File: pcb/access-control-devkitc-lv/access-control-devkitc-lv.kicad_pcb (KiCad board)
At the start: 2 copper layers, 71.4 x 65.5 mm, 41 parts, among them J1 CON_I2C, K1 G5LE-1, U1 ESP32-DevKitC

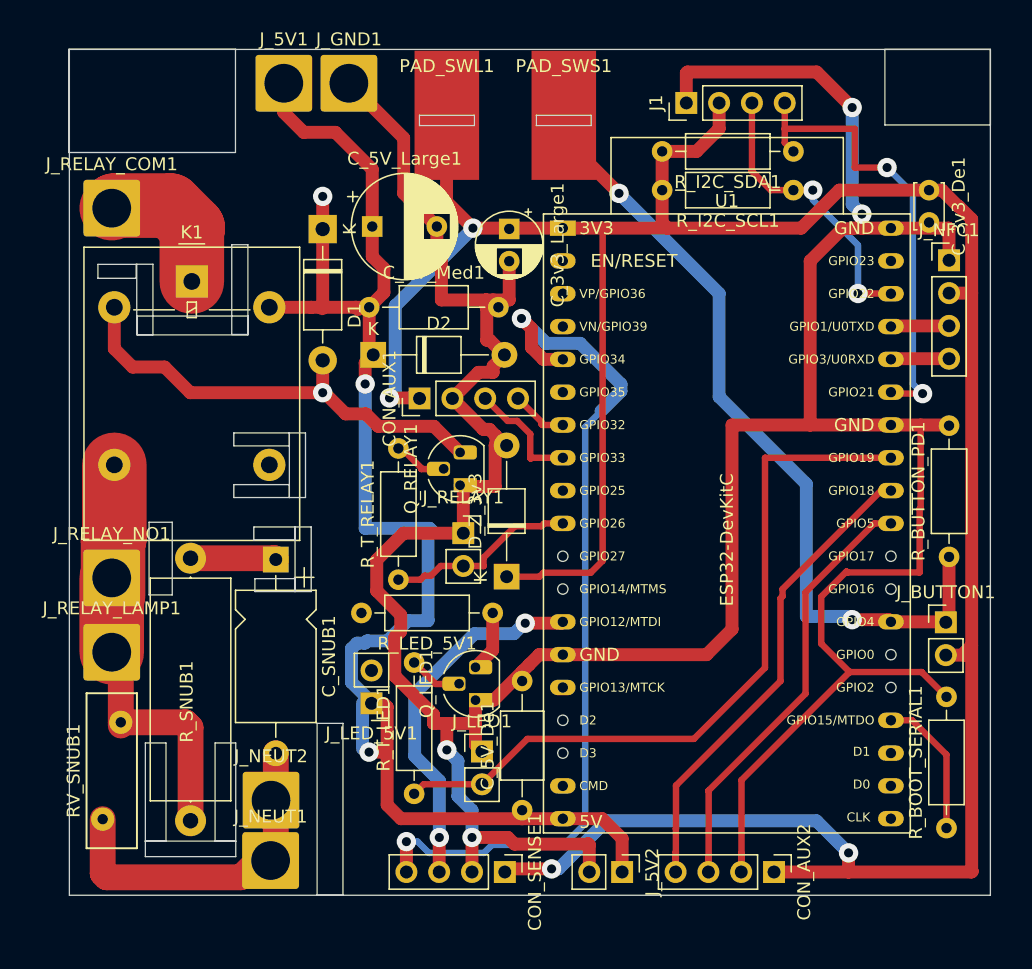
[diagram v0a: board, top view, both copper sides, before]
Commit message: Split board into Low Voltage / Relay modules
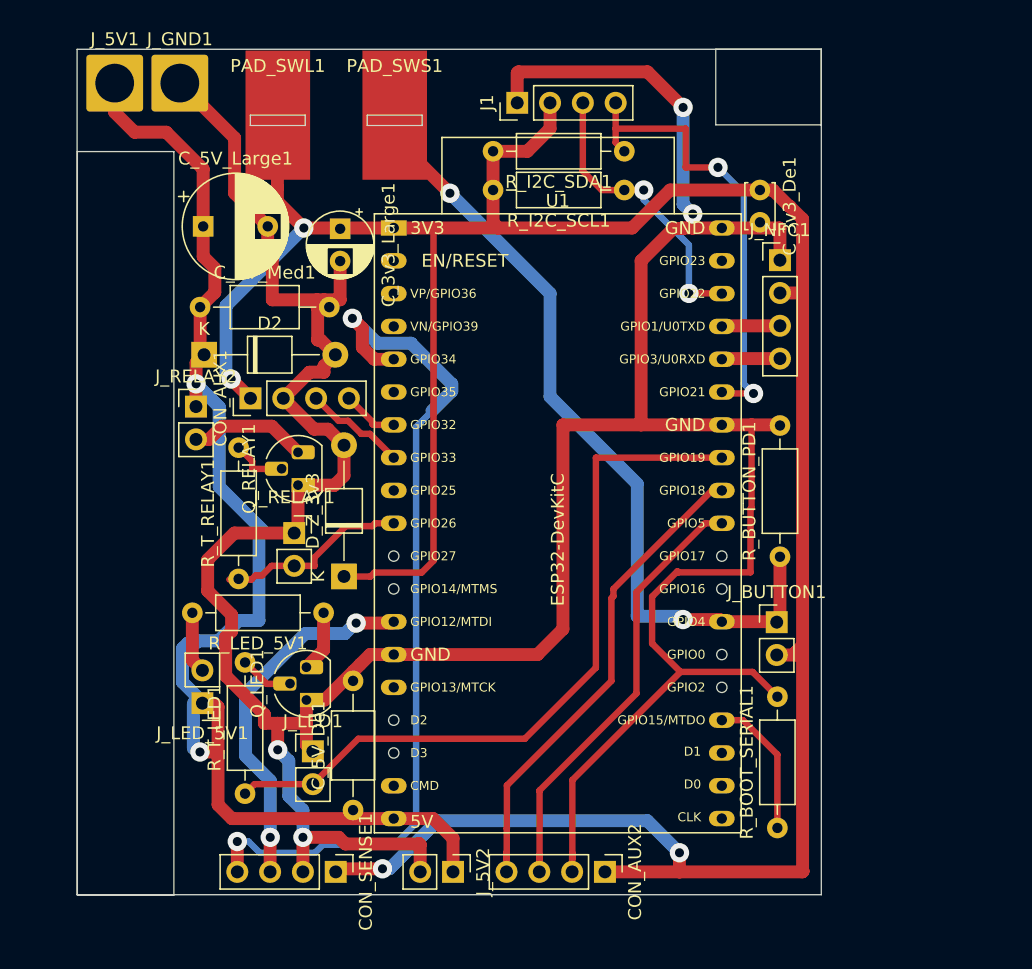
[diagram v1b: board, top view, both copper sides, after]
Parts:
- removed C_SNUB1: C, Capacitor_THT:CP_Axial_L10.0mm_D6.0mm_P15.00mm_Horizontal
- removed D1: 1N4007, Diode_THT:D_DO-41_SOD81_P10.16mm_Horizontal
- removed J_NEUT1, J_NEUT2, J_RELAY_COM1, J_RELAY_LAMP1, J_RELAY_NO1: Conn_01x01_Socket, Connector_Wire:SolderWire-2.5sqmm_1x01_D2.4mm_OD4.4mm
- removed K1: G5LE-1, Relay_THT:Relay_SPDT_Omron-G5LE-1
- removed RV_SNUB1: Varistor, Varistor:RV_Disc_D12mm_W3.9mm_P7.5mm
- removed R_SNUB1: R, Resistor_THT:R_Axial_DIN0617_L17.0mm_D6.0mm_P20.32mm_Horizontal
- added J_RELAY2: Conn_01x02_Socket, Connector_PinHeader_2.54mm:PinHeader_1x02_P2.54mm_Vertical, F.Cu at (9.20, 27.6)
- moved CON_AUX2 13.1 mm to (40.9, 63.7)
- moved C_3v3_De1 13.1 mm to (52.9, 10.9)
- moved C_3v3_Large1 13.1 mm to (20.4, 13.9)
- moved C_5V_De1 13.1 mm to (21.4, 58.9)
- moved J_BUTTON1 13.1 mm to (54.2, 44.3)
- moved J_NFC1 13.1 mm to (54.4, 16.3)
- moved R_BUTTON_PD1 13.1 mm to (54.4, 39.3)
- moved R_I2C_SCL1 13.1 mm to (42.4, 10.9)
- moved R_I2C_SDA1 13.1 mm to (42.4, 7.88)
- moved R_LED_5V1 13.1 mm to (19.1, 43.6)
- moved CON_AUX1 13.1 mm to (13.4, 27.0)
- moved C_5V_Large1 13.1 mm to (9.76, 13.7)
- moved D2 13.1 mm to (9.83, 23.6)
- moved CON_SENSE1 13.1 mm to (20.0, 63.7)
- moved C_5V_Med1 13.1 mm to (9.52, 19.9)
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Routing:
- net Net-(J_RELAY_LAMP1-Pin_1): track 36.5 -> 0.00 mm
- net Net-(J_RELAY2-Pin_2): track 35.8 -> 9.16 mm, vias 1 -> 0
- net NEUT: track 25.0 -> 0.00 mm
- net +5V: track 116.2 -> 98.3 mm, vias 3 -> 2
- net Net-(J_RELAY_COM1-Pin_1): track 11.2 -> 0.00 mm
- net Net-(C_SNUB1-Pad1): track 6.78 -> 0.00 mm
- net Net-(J_LED_5V1-Pin_2): track 0.00 -> 4.78 mm
- net +3V3: track 215.8 -> 214.1 mm
- net GND: track 270.1 -> 271.4 mm
- net Net-(CON_AUX1-Pin_3): track 9.06 -> 7.91 mm
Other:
- board size 71.4 x 65.5 mm -> 57.6 x 65.5 mm

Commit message: Update with values
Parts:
- removed J_GND1: Conn_01x01_Socket, Connector_Wire:SolderWire-2.5sqmm_1x01_D2.4mm_OD4.4mm
- C_5V_De1: footprint Capacitor_THT:C_Axial_L5.1mm_D3.1mm_P10.00mm_Horizontal -> Capacitor_THT:C_Disc_D4.3mm_W1.9mm_P5.00mm
- C_5V_Med1: footprint Capacitor_THT:C_Axial_L5.1mm_D3.1mm_P10.00mm_Horizontal -> Capacitor_THT:C_Disc_D5.0mm_W2.5mm_P5.00mm
- J_5V1: value Conn_01x01_Socket -> Conn_01x02_Socket; footprint Connector_Wire:SolderWire-2.5sqmm_1x01_D2.4mm_OD4.4mm -> Connector_PinHeader_2.54mm:PinHeader_1x02_P2.54mm_Vertical
- J_RELAY2: footprint Connector_PinHeader_2.54mm:PinHeader_1x02_P2.54mm_Vertical -> Connector_PinHeader_2.54mm:PinHeader_1x04_P2.54mm_Vertical
- moved C_5V_De1 7.65 mm to (14.1, 56.6)
- moved J1 7.44 mm to (26.6, 4.22)
- moved J_5V2 7.44 mm to (21.7, 63.8)
- moved PAD_SWS1 7.44 mm to (17.1, 5.18)
- moved Q_RELAY1 7.44 mm to (9.66, 33.8)
- moved U1 7.44 mm to (17.1, 13.9)
- moved CON_AUX1 7.44 mm to (5.98, 27.1)
- moved CON_SENSE1 7.44 mm to (12.6, 63.8)
- moved C_3v3_Large1 7.44 mm to (12.9, 14.0)
- moved C_5V_Large1 7.44 mm to (2.32, 13.8)
- moved C_5V_Med1 7.44 mm to (2.08, 20.0)
- moved D2 7.44 mm to (2.39, 23.7)
- moved D_Z_3v3 7.44 mm to (13.2, 40.9)
- moved J_LED1 7.44 mm to (10.8, 54.4)
- moved J_LED_5V1 7.44 mm to (2.26, 50.7)
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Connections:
- Q_RELAY1 pad 2: Net-(Q_RELAY1-B) -> Net-(J_RELAY2-Pin_3)
- R_T_RELAY1 pad 2: Net-(Q_RELAY1-B) -> Net-(J_RELAY2-Pin_3)
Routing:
- net Net-(J_RELAY2-Pin_3): track 0.00 -> 7.84 mm
- net +5V: track 98.3 -> 91.4 mm
- net GND: track 271.4 -> 277.5 mm
- net Net-(Q_RELAY1-B): track 3.83 -> 0.00 mm
- net +3V3: track 214.1 -> 212.5 mm
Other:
- board size 57.6 x 65.5 mm -> 50.1 x 65.5 mm

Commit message: Updates for manufacturing
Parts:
- PAD_SWL1, PAD_SWS1: moved to B.Cu
- R_BOOT_SERIAL1, R_BUTTON_PD1: value R -> 10kR
- R_LED_5V1: value R -> 330R
- turned PAD_SWL1 to 180 degrees
- turned PAD_SWS1 to 180 degrees
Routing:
- net Net-(J_BUTTON1-Pin_1): track 62.1 -> 59.4 mm, vias 2 -> 3
- net +3V3: track 212.5 -> 210.2 mm, vias 4 -> 5
